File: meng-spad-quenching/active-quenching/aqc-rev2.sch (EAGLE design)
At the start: 289 parts, among them IC1 ADCMP582, IC10 74AHC1G04DBV, IC11 74AHC1G04DBV, IC12 TLV272DGK, IC13 TLV271DBV, IC14 74AHC1G04DBV, IC15 ALD1106, IC16 ALD1107, IC17 74AHC1G04DBV, IC18 LT1534-1, IC19 LT1534-1, IC2 TLV271DBV, IC20 STM32F411RE, IC22 TPS7A3001, IC24 TPS7A4901, IC25 TPS7A4901, IC27 USBLC6-2SC6Y, IC28 MAX572X, IC3 NC7SV74K8X, IC4 TLV272DGK, IC5 NC7WZ16P6X, IC6 LTC1711, IC7 DS1100LU-20+, IC8 LM1117, M1 BSS806N, M2 BSS806N, M3 BSS806N, Q1 IRLML6402TRPBF, Q2 MMBTH81, Q3 MMBTH81, Q5 MMBTH81, Q7 MMBTH81, Q8 MMBTH81, T1 MMBTH10, T2 MMBTH10, T5 MMBTH10, T6 MMBTH10, T7 MMBTH10, T8 MMBTH10, T9 MMBTH10, U1 SN65EPT21DGK, U2 SN65EPT22DGK, X1 CONN_SPAD, X2 CONN_PHOTON_COUNTER, X3 KEYSTONE-7774, X4 KEYSTONE-7774, X5 CONN_SMU, X6 CONN_FORCE_QUENCH, X7 CONN_PULLDN_SENSE, X8 PN61729-S

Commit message: Prelim. placement of starved inverter
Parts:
- C55: device rcl:C-EUC0402 -> rcl:C-EUC0603
- TP4, TP5, TP6, TP8, TP9: value TPTP20R -> TPTP15R; device testpad:TPTP20R -> testpad:TPTP15R
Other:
- note added: "Film"
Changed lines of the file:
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@@
 <setting verticaltext="up"/>
 </settings>
-<grid distance="0.1" unitdist="inch" unit="inch" style="lines" multiple="1" display="yes" altdistance="0.01" altunitdist="inch" altunit="inch"/>
+<grid distance="0.1" unitdist="inch" unit="inch" style="lines" multiple="1" display="no" altdistance="0.01" altunitdist="inch" altunit="inch"/>
 <layers>
 <layer number="1" name="Top" color="4" fill="1" visible="yes" active="no"/>
@@
 <part name="H4" library="holes" deviceset="MOUNT-PAD-ROUND" device="3.2"/>
 <part name="GND37" library="supply1" deviceset="GND" device=""/>
-<part name="TP9" library="testpad" deviceset="TP" device="TP20R"/>
-<part name="TP5" library="testpad" deviceset="TP" device="TP20R"/>
-<part name="TP6" library="testpad" deviceset="TP" device="TP20R"/>
+<part name="TP9" library="testpad" deviceset="TP" device="TP15R" value="TPTP15R"/>
+<part name="TP5" library="testpad" deviceset="TP" device="TP15R" value="TPTP15R"/>
+<part name="TP6" library="testpad" deviceset="TP" device="TP15R" value="TPTP15R"/>
 <part name="IC3" library="meng" deviceset="NC7SV74K8X" device="" value="NC7SV74K8X"/>
 <part name="R1" library="rcl" deviceset="R-EU_" device="R0603" value="DNP"/>
@@
 <part name="R34" library="rcl" deviceset="R-EU_" device="R0603" value="DNP"/>
 <part name="DNP17" library="meng" deviceset="ARROW_1DIR" device=""/>
-<part name="TP8" library="testpad" deviceset="TP" device="TP20R"/>
+<part name="TP8" library="testpad" deviceset="TP" device="TP15R" value="TPTP15R"/>
 <part name="DNP42" library="meng" deviceset="ARROW_1DIR" device=""/>
 <part name="DNP48" library="meng" deviceset="ARROW_1DIR" device=""/>
@@
 <part name="DNP1" library="meng" deviceset="ARROW_1DIR" device=""/>
 <part name="DNP49" library="meng" deviceset="ARROW_1DIR" device=""/>
-<part name="TP4" library="testpad" deviceset="TP" device="TP20R">
+<part name="TP4" library="testpad" deviceset="TP" device="TP15R" value="TPTP15R">
 <attribute name="TP_SIGNAL_NAME" value=""/>
 </part>
@@
 <part name="IC14" library="74xx-little-de" deviceset="74*1G04" device="DBV" technology="AHC"/>
 <part name="GND94" library="supply1" deviceset="GND" device=""/>
-<part name="C55" library="rcl" deviceset="C-EU" device="C0402" value="10p"/>
+<part name="C55" library="rcl" deviceset="C-EU" device="C0603" value="10p"/>
 <part name="DNP78" library="meng" deviceset="ARROW_1DIR" device=""/>
 <part name="T9" library="transistor" deviceset="*-NPN-" device="SOT23-BEC" technology="MMBTH10LT1" value="MMBTH10"/>
@@
 <text x="266.7" y="8.255" size="2.54" layer="97" font="vector" align="center">2.0</text>
 <text x="223.52" y="8.255" size="3.81" layer="97" font="vector" align="center">1 of 1</text>
+<text x="93.98" y="124.46" size="1.778" layer="98">Film</text>
+<text x="210.82" y="124.46" size="1.778" layer="98">Film</text>
 </plain>
 <instances>

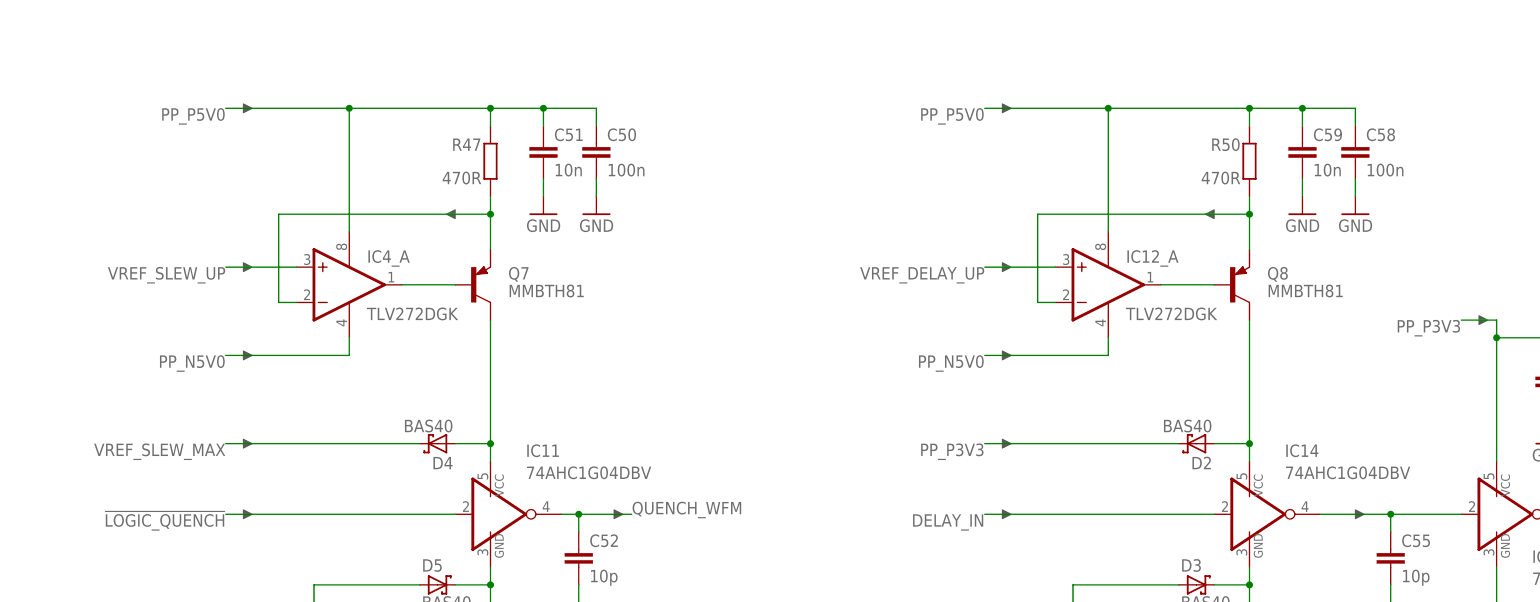
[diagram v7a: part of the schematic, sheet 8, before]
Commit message: More layout, added 470pF caps to slew diodes
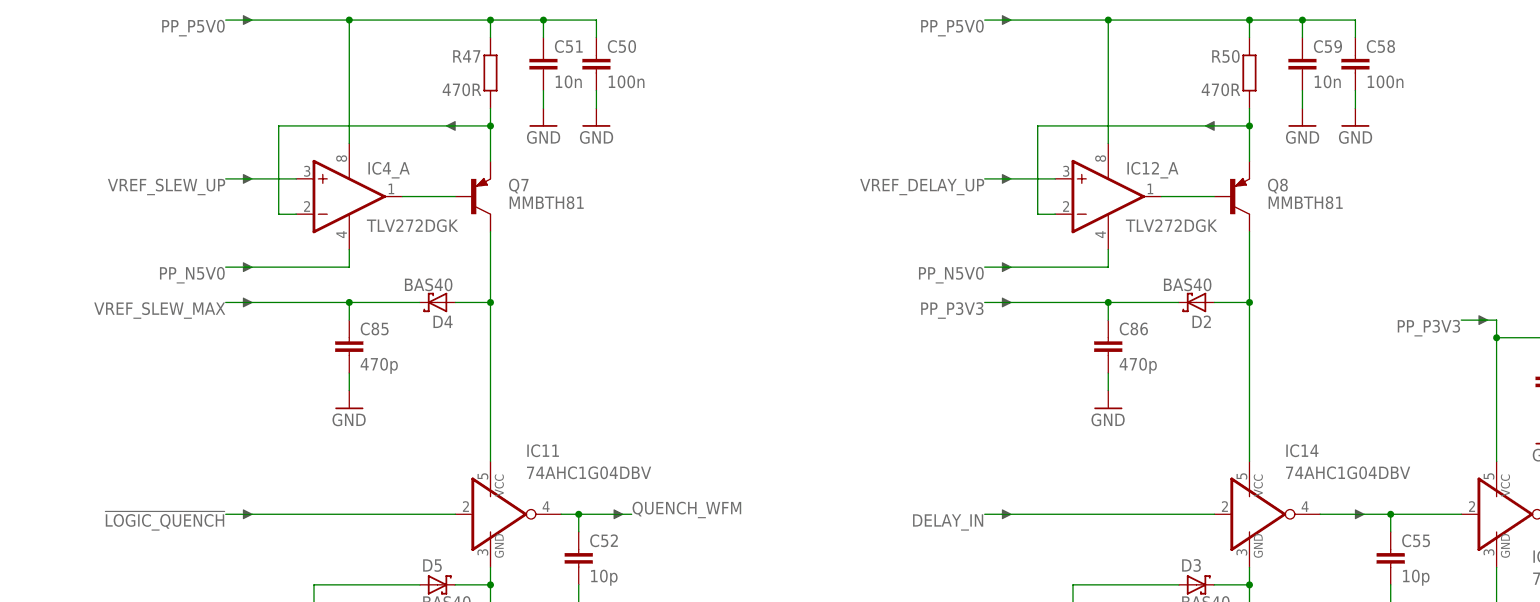
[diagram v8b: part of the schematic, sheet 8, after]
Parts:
- added C85, C86: 470p, rcl:C-EUC0603
- added TP7: TPTP06R, testpad:TPTP06R
- TP1: value TPTP08R -> TPTP06R; device testpad:TPTP08R -> testpad:TPTP06R
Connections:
- net GND: now also C85.2, C86.2
- net LOGIC_QUENCH: now also TP7.TP
- net PP_P3V3: now also C86.1
- net VREF_SLEW_MAX: now also C85.1
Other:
- moved on the sheet: C50, C51, C58, C59, D2, D4, IC12_A, IC4_A, Q7, Q8, R47, R50
